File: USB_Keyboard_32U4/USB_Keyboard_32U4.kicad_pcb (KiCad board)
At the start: 2 copper layers, 31 x 33.5 mm, 22 parts, among them J1 USB_C_Receptacle_USB2.0_16P, J2 Conn_02x03_Odd_Even, U1 ATmega32U4-A, Y1 16MHz

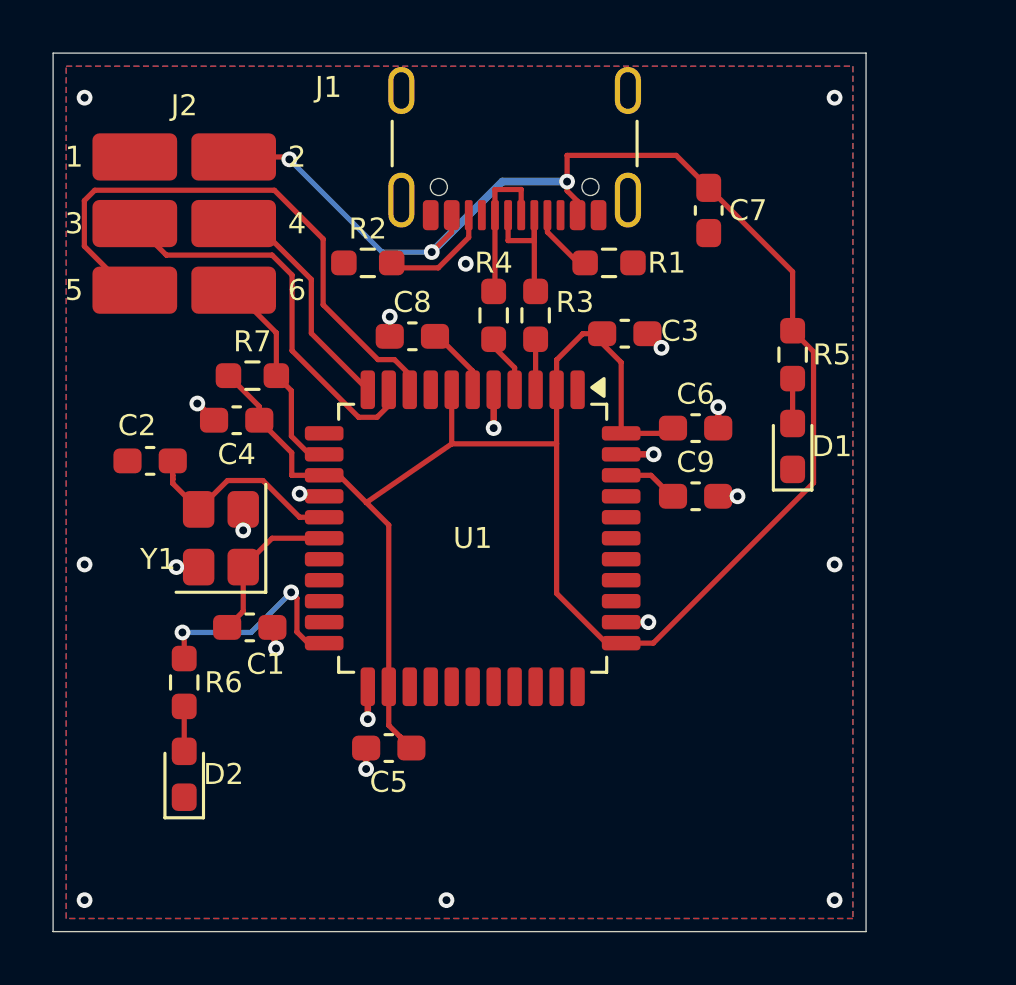
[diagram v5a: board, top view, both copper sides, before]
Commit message: Finalize PCB layout for fabrication
Move the ISP pogo pads to the board underside, add manufacturing-adjusted USB-C and ISP footprints, and refine routing, outline, silkscreen, and design rules. Remove intermediate layout files while retaining final-board verification and relocation records.
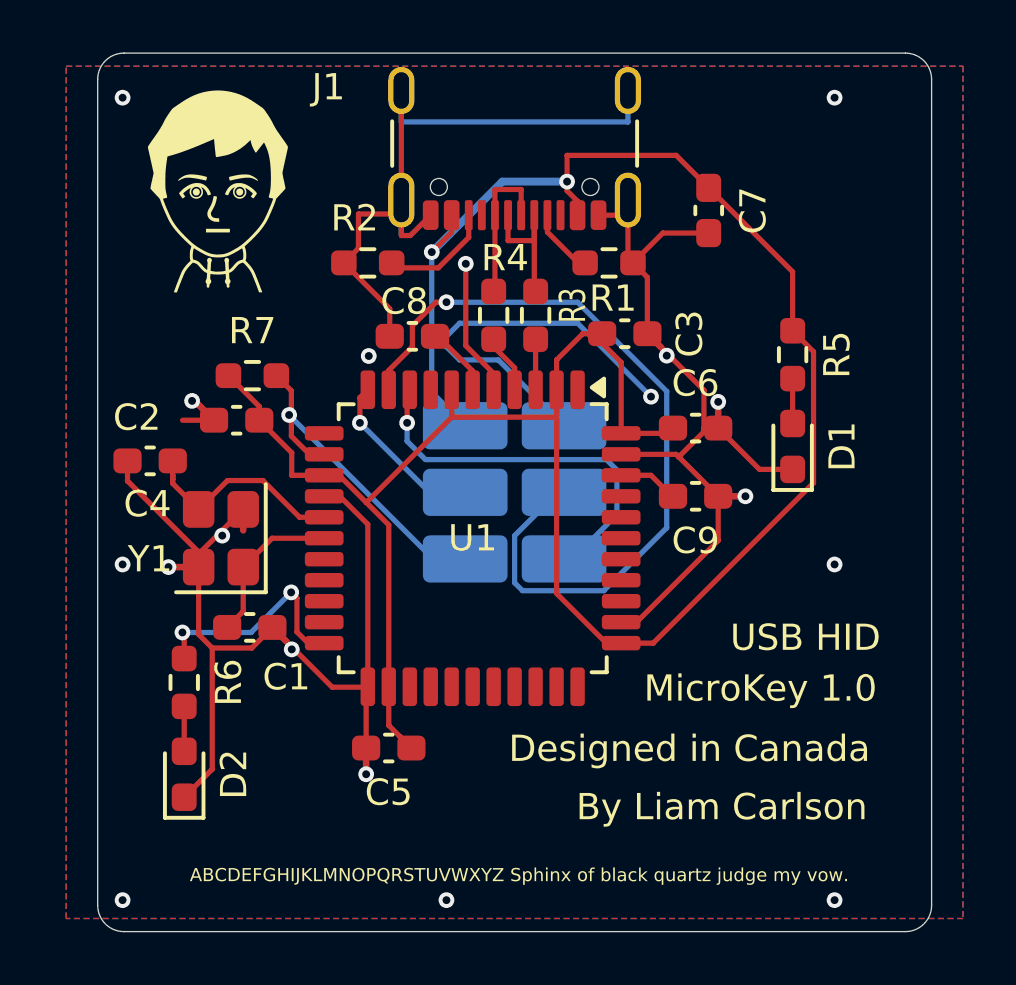
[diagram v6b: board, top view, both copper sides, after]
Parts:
- added G***: LOGO, Custom Footprints:MIIImage 8.25mm, F.Cu at (106.2, 104.5)
- J1: footprint Connector_USB:USB_C_Receptacle_GCT_USB4105-xx-A_16P_TopMnt_Horizontal -> MicroKey_Local:USB4105_JLC_0p20mm_NPTH_Clearance
- J2: footprint 2x3 Pads:MicroKey_AVR_ISP_2x3_SMD -> MicroKey_Local:AVR_ISP_2x3_Pogo_3p23x1p80; moved to B.Cu
- moved J2 16.2 mm to (117.6, 116.2), turned to 180 degrees
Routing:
- net GND: track 13.1 -> 120.5 mm, vias 22 -> 18
- net PB2: track 15.2 -> 30.8 mm, vias 0 -> 1
- net PB1: track 21.9 -> 14.9 mm, vias 0 -> 1
- net RESET: track 8.02 -> 13.2 mm, vias 0 -> 1
- net PB3: track 8.94 -> 6.50 mm, vias 0 -> 1
- net VCC: track 97.6 -> 95.3 mm, vias 3 -> 2
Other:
- board size 31 x 33.5 mm -> 31.8 x 33.5 mm
- board text added: "ABCDEFGHIJKLMNOPQRSTUVWXYZ Sphinx of black quartz judge my vow."
- board text added: "By Liam Carlson"
- board text added: "Designed in Canada"
- board text added: "GND"
- board text added: "MicroKey 1.0"
- board text added: "PB1"
- board text added: "PB2"
- board text added: "PB3"
- board text added: "RESET"
- board text added: "USB HID"
- board text added: "VCC"
- board text removed: "1"
- board text removed: "2"
- board text removed: "3"
- board text removed: "4"
- board text removed: "5"
- board text removed: "6"

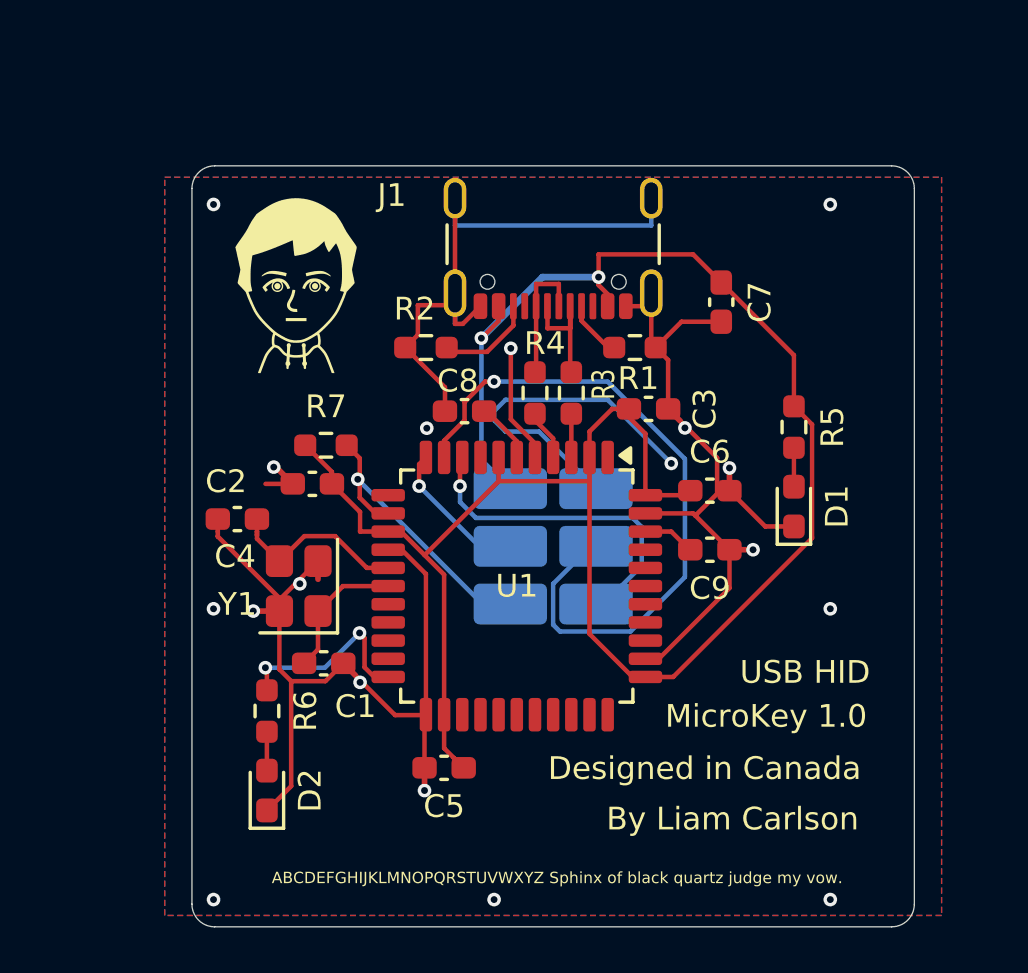
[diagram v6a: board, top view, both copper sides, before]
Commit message: Redesign USB keyboard PCB layout
Reposition components and reroute the board for the revised outline, move the AVR ISP pogo pads to the front, and update silkscreen labeling.
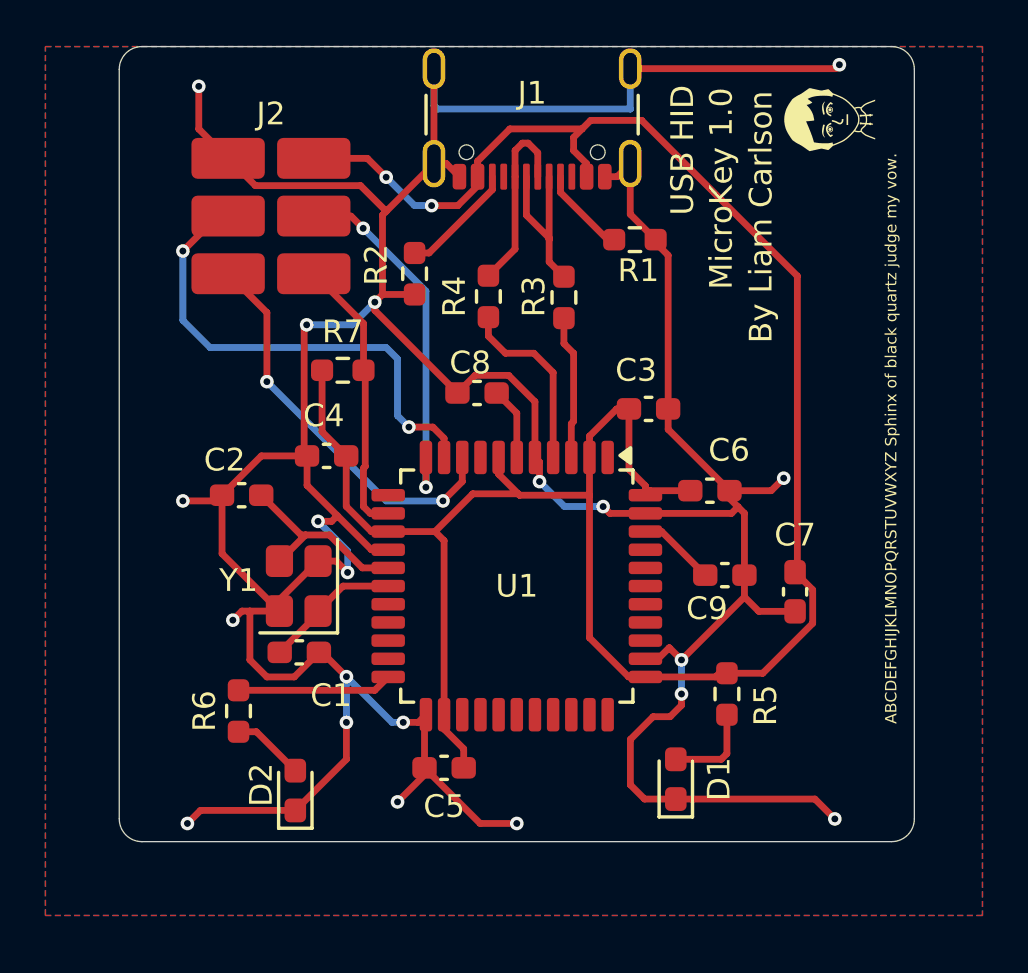
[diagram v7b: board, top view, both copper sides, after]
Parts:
- J2: moved to F.Cu
- moved mii 24.3 mm to (129.5, 97.5), turned to 90 degrees
- moved J2 19.1 mm to (105.2, 101.7), turned to 0 degrees
- moved C7 13.2 mm to (128.2, 118.2)
- moved D1 13.1 mm to (123.0, 126.5)
- moved R5 12.1 mm to (125.2, 122.8)
- moved J1 5.78 mm to (116.7, 96.3)
- moved R1 4.75 mm to (121.2, 102.8)
- moved R4 4.72 mm to (114.8, 105.2)
- moved R3 4.22 mm to (118.1, 105.3)
- moved R7 3.38 mm to (108.3, 108.5)
- moved R2 3.29 mm to (111.5, 104.2), turned to -90 degrees
- moved C4 1.38 mm to (107.6, 112.3)
- moved C9 1.30 mm to (125.2, 117.5)
- moved D2 1.25 mm to (106.2, 127.0)
- moved R6 1.25 mm to (103.8, 123.5)
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- renumbered G*** to mii
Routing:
- net GND: track 120.5 -> 191.6 mm, vias 18 -> 20
- net VCC: track 95.3 -> 105.4 mm
- net PB3: track 6.50 -> 16.3 mm, vias 1 -> 2
- net PB2: track 30.8 -> 21.6 mm, vias 1 -> 2
- net D+: track 2.26 -> 8.09 mm
- net D-: track 1.93 -> 6.35 mm
- net PB1: track 14.9 -> 17.6 mm, vias 1 -> 2
- net Net-(J1-D+-PadA6): track 5.92 -> 8.36 mm
- net Net-(D1-A): track 1.71 -> 4.07 mm
- net Net-(J1-D--PadA7): track 5.90 -> 7.86 mm
- net Net-(U1-PD5): track 8.62 -> 6.83 mm, vias 2 -> 0
- net Net-(D2-A): track 1.71 -> 3.21 mm
- net Net-(J1-CC1): track 2.57 -> 3.92 mm
- net Net-(U1-AREF): track 2.31 -> 3.43 mm
- net Net-(J1-CC2): track 4.35 -> 5.15 mm
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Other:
- board size 31.8 x 33.5 mm -> 35 x 35 mm
- board text removed: "Designed in Canada"
- board text removed: "GND"
- board text removed: "PB1"
- board text removed: "PB2"
- board text removed: "PB3"
- board text removed: "RESET"
- board text removed: "VCC"

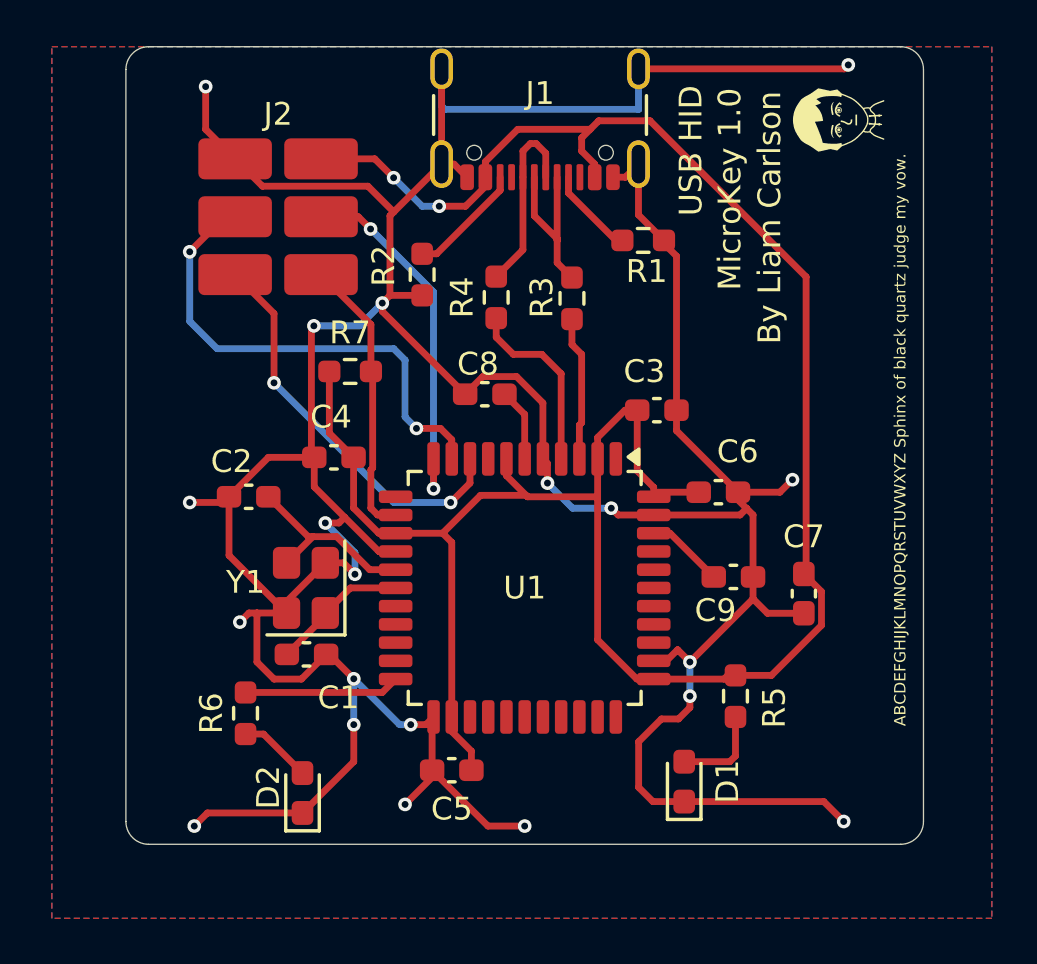
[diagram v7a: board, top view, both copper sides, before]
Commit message: Revise 32U4 PCB layout and silkscreen
Rework component placement and routing, refill copper zones, and add a local MicroKey logo plus a Lucide keyboard silkscreen footprint with its ISC license.
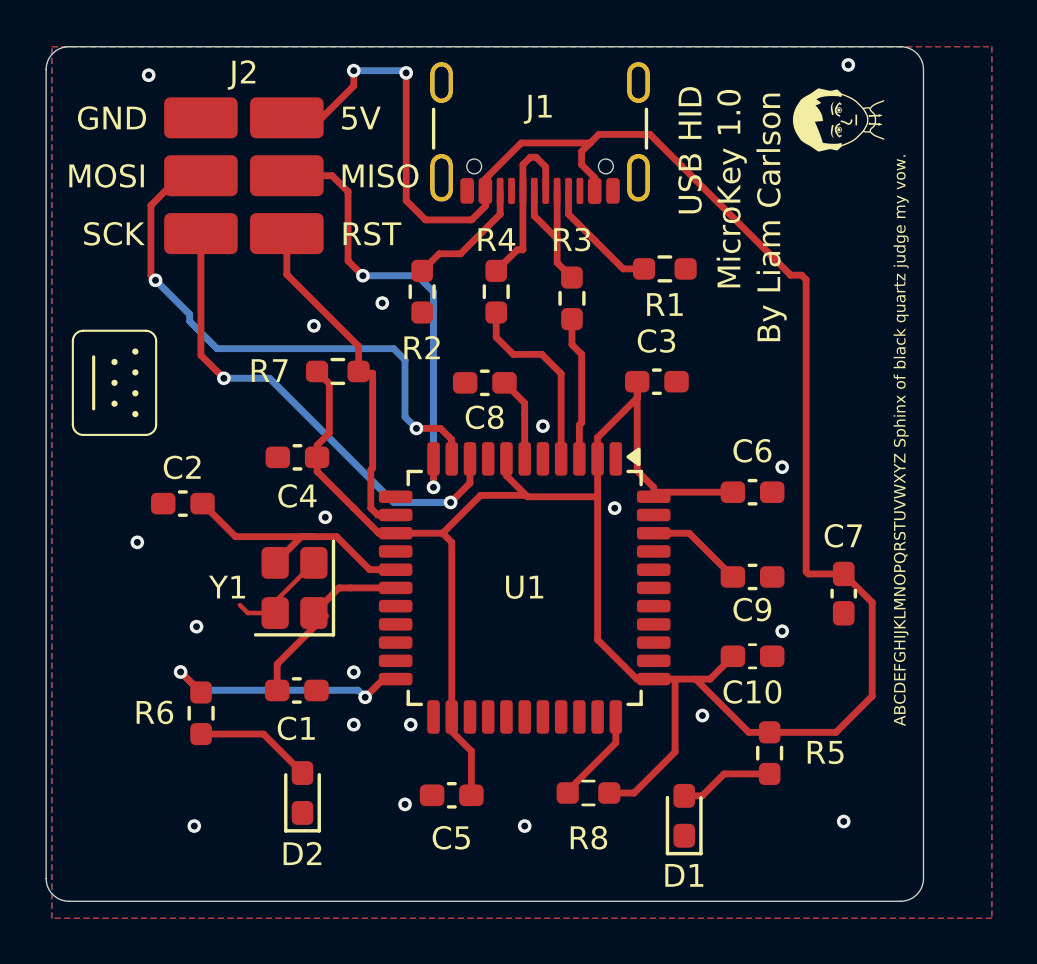
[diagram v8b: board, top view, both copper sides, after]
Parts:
- added C10: 100nF, Capacitor_SMD:C_0603_1608Metric_Pad1.08x0.95mm_HandSolder, F.Cu at (126.0, 121.0)
- added GKB1: Keyboard_Lucide_10mm_Silkscreen, MicroKey_Local:Keyboard_Lucide_10mm_Silkscreen, F.Cu at (98.0, 109.0)
- added R8: 10k, Resistor_SMD:R_0603_1608Metric_Pad0.98x0.95mm_HandSolder, F.Cu at (118.8, 127.0)
- mii: footprint Custom Footprints:MIIImage 8.25mm -> MicroKey_Local:MicroKey_Logo
- moved R5 2.92 mm to (126.8, 125.2)
- moved C2 2.90 mm to (101.0, 114.3)
- moved J2 2.34 mm to (103.7, 99.9)
- moved R6 1.95 mm to (101.8, 123.5)
- moved C7 1.75 mm to (130.0, 118.2)
- moved C1 1.64 mm to (106.0, 122.5)
- moved C4 1.60 mm to (106.0, 112.3)
- moved R1 1.57 mm to (122.2, 104.0)
- moved C6 1.50 mm to (126.0, 113.8)
- moved D1 1.50 mm to (123.0, 128.0)
- moved C3 1.25 mm to (121.8, 109.0)
- moved C5 1.10 mm to (112.8, 127.1)
- moved C9 0.84 mm to (126.0, 117.5)
- moved R2 0.75 mm to (111.5, 105.0)
- moved J1 0.60 mm to (116.7, 96.9)
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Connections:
- U1 pad 33: unconnected-(U1-~{HWB}/PE2-Pad33) -> HWB
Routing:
- net GND: track 191.6 -> 4.60 mm, vias 20 -> 19
- net VCC: track 105.4 -> 135.1 mm
- net Net-(U1-PD5): track 6.83 -> 11.5 mm, vias 0 -> 2
- net HWB: track 0.00 -> 4.21 mm
- net PB3: track 16.3 -> 20.2 mm
- net PB1: track 17.6 -> 21.2 mm
- net Net-(U1-XTAL2): track 8.54 -> 11.8 mm
- net PB2: track 21.6 -> 24.5 mm
- net RESET: track 12.4 -> 15.2 mm
- net Net-(U1-XTAL1): track 6.06 -> 8.74 mm
- net Net-(D2-A): track 3.21 -> 5.16 mm
- net Net-(J1-CC1): track 3.92 -> 5.33 mm
- net Net-(J1-D--PadA7): track 7.86 -> 6.66 mm
- net Net-(U1-AREF): track 3.43 -> 4.27 mm
- net Net-(J1-D+-PadA6): track 8.36 -> 7.66 mm
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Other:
- board size 35 x 35 mm -> 38.5 x 37.5 mm
- board text added: "5V"
- board text added: "GND"
- board text added: "MISO"
- board text added: "MOSI"
- board text added: "RST"
- board text added: "SCK"
